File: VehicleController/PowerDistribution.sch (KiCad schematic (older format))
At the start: 22 parts, among them P3 RPi_USB_PWR, U10 BTS6133D, U11 R-78E5.0-1.0, U9 TL431

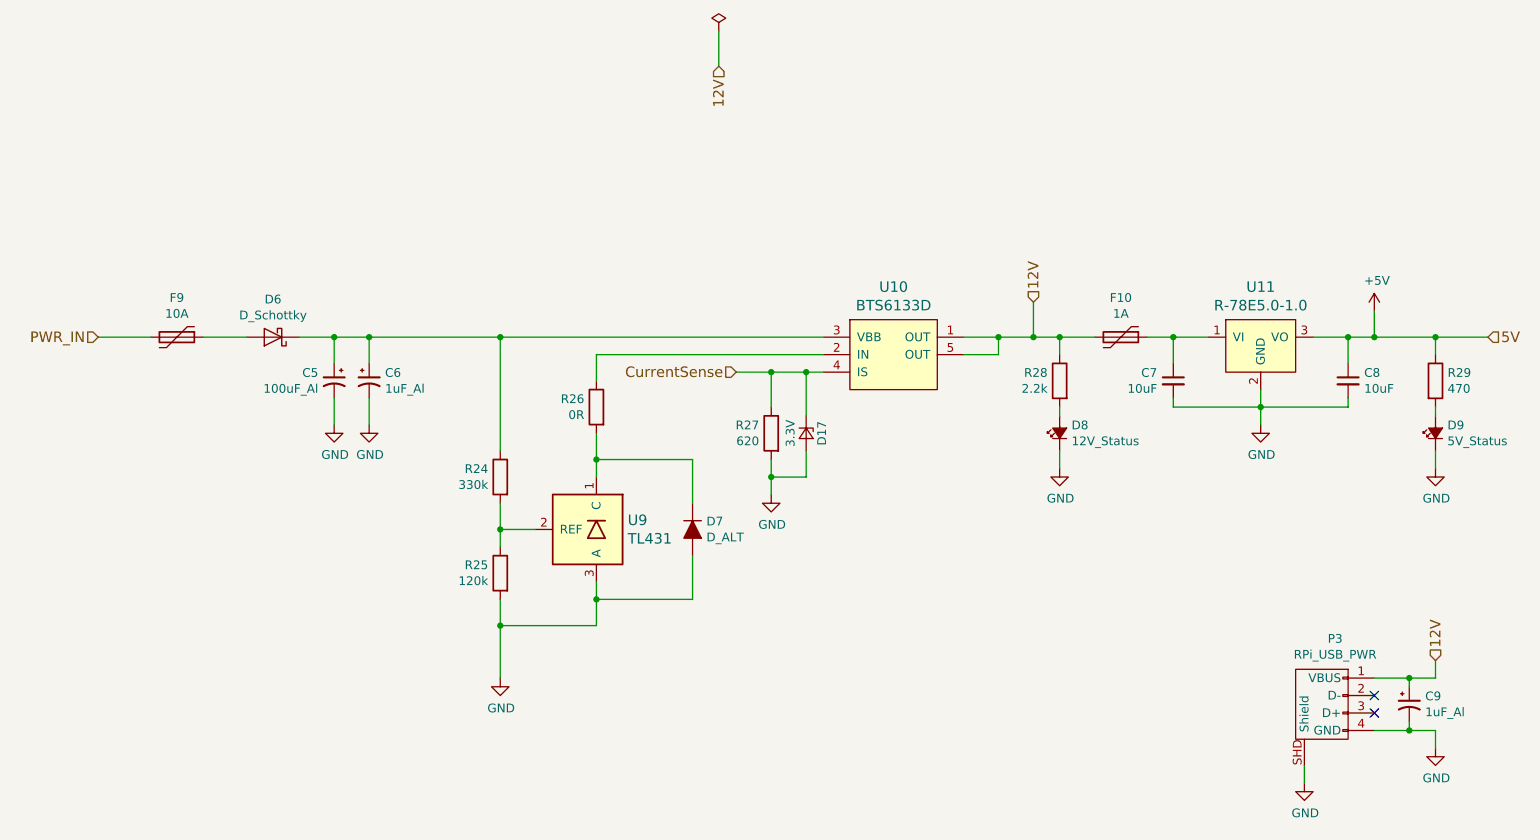
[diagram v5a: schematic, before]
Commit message: Fix Motor Controller Override circuit, better net names
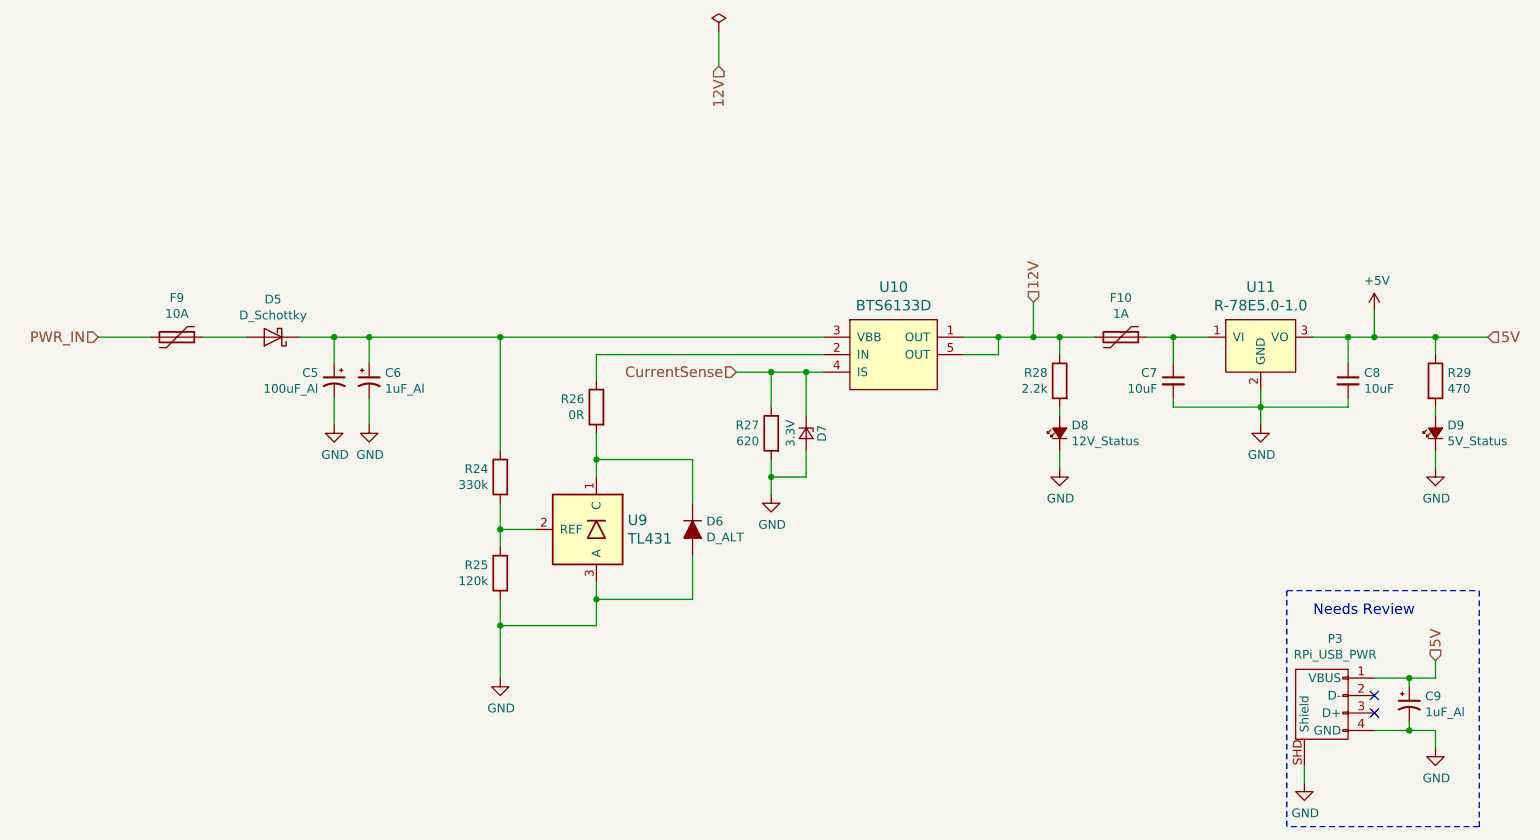
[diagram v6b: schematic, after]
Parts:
- renumbered D6 to D5, D7 to D6, D17 to D7
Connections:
- net +5V: now also C9.1, P3.1 (VBUS)
- net 12V: no longer C9.1, P3.1 (VBUS)
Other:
- note added: "Needs Review"
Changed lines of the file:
@@
 $EndDescr
 $Comp
-L D_Schottky D6
+L D_Schottky D5
 U 1 1 587C7BB2
 P 3000 2750
-F 0 "D6" H 3000 2534 50  0000 C CNN
+F 0 "D5" H 3000 2534 50  0000 C CNN
 F 1 "D_Schottky" H 3000 2625 50  0000 C CNN
 F 2 "Diodes_SMD:SMA_Handsoldering" H 3000 2750 50  0001 C CNN
@@
 $EndComp
 $Comp
-L GND #PWR41
+L GND #PWR042
 U 1 1 587C7BE3
 P 5850 3650
-F 0 "#PWR41" H 5850 3400 50  0001 C CNN
+F 0 "#PWR042" H 5850 3400 50  0001 C CNN
 F 1 "GND" H 5855 3477 50  0000 C CNN
 F 2 "" H 5850 3650 50  0000 C CNN
@@
 $EndComp
 $Comp
-L GND #PWR40
+L GND #PWR043
 U 1 1 587C7BF7
 P 4300 4700
-F 0 "#PWR40" H 4300 4450 50  0001 C CNN
+F 0 "#PWR043" H 4300 4450 50  0001 C CNN
 F 1 "GND" H 4305 4527 50  0000 C CNN
 F 2 "" H 4300 4700 50  0000 C CNN
@@
 $EndComp
 $Comp
-L GND #PWR43
+L GND #PWR044
 U 1 1 58AEB860
 P 8650 3250
-F 0 "#PWR43" H 8650 3000 50  0001 C CNN
+F 0 "#PWR044" H 8650 3000 50  0001 C CNN
 F 1 "GND" H 8655 3077 50  0000 C CNN
 F 2 "" H 8650 3250 50  0000 C CNN
@@
 5V
 $Comp
-L PWR_FLAG #FLG3
+L PWR_FLAG #FLG045
 U 1 1 58AF2028
 P 5550 1000
-F 0 "#FLG3" H 5550 1095 50  0001 C CNN
+F 0 "#FLG045" H 5550 1095 50  0001 C CNN
 F 1 "PWR_FLAG" H 5550 1224 50  0001 C CNN
 F 2 "" H 5550 1000 50  0000 C CNN
@@
 $EndComp
 $Comp
-L GND #PWR44
+L GND #PWR046
 U 1 1 58B30D9F
 P 8900 5300
-F 0 "#PWR44" H 8900 5050 50  0001 C CNN
+F 0 "#PWR046" H 8900 5050 50  0001 C CNN
 F 1 "GND" H 8905 5127 50  0000 C CNN
 F 2 "" H 8900 5300 50  0000 C CNN
@@
 NoConn ~ 9300 4800
 NoConn ~ 9300 4900
-Text HLabel 9650 4600 1    60   Input ~ 0
-12V
-$Comp
-L GND #PWR47
+$Comp
+L GND #PWR047
 U 1 1 58B31164
 P 9650 5100
-F 0 "#PWR47" H 9650 4850 50  0001 C CNN
+F 0 "#PWR047" H 9650 4850 50  0001 C CNN
 F 1 "GND" H 9655 4927 50  0000 C CNN
 F 2 "" H 9650 5100 50  0000 C CNN
@@
 $EndComp
 $Comp
-L GND #PWR38
+L GND #PWR048
 U 1 1 58B0EFE3
 P 3350 3250
-F 0 "#PWR38" H 3350 3000 50  0001 C CNN
+F 0 "#PWR048" H 3350 3000 50  0001 C CNN
 F 1 "GND" H 3355 3077 50  0000 C CNN
 F 2 "" H 3350 3250 50  0000 C CNN
@@
 $EndComp
 $Comp
-L GND #PWR39
+L GND #PWR049
 U 1 1 58B0F09D
 P 3550 3250
-F 0 "#PWR39" H 3550 3000 50  0001 C CNN
+F 0 "#PWR049" H 3550 3000 50  0001 C CNN
 F 1 "GND" H 3555 3077 50  0000 C CNN
 F 2 "" H 3550 3250 50  0000 C CNN
@@
 $EndComp
 $Comp
-L D_ALT D7
+L D_ALT D6
 U 1 1 58B90308
 P 5400 3850
-F 0 "D7" V 5354 3929 50  0000 L CNN
+F 0 "D6" V 5354 3929 50  0000 L CNN
 F 1 "D_ALT" V 5445 3929 50  0000 L CNN
 F 2 "Diodes_SMD:SMA_Handsoldering" H 5400 3850 50  0001 C CNN
@@
 	0    1    1    0
 $EndComp
-Wire Wire Line
-	5850 3150 5850 2950
-Wire Wire Line
-	5650 2950 6150 2950
-Wire Wire Line
-	4850 2850 6150 2850
-Wire Wire Line
-	3150 2750 6150 2750
-Wire Wire Line
-	4300 2750 4300 3400
-Connection ~ 4300 2750
-Wire Wire Line
-	5850 3450 5850 3650
-Wire Wire Line
-	4300 3700 4300 3950
-Wire Wire Line
-	4500 3850 4300 3850
-Connection ~ 4300 3850
-Wire Wire Line
-	2600 2750 2850 2750
-Wire Wire Line
-	2000 2750 2300 2750
-Wire Wire Line
-	4300 4250 4300 4700
-Wire Wire Line
-	4850 4400 4300 4400
-Wire Wire Line
-	4850 4150 4850 4400
-Connection ~ 4300 4400
-Wire Wire Line
-	6950 2850 7150 2850
-Wire Wire Line
-	7150 2850 7150 2750
-Connection ~ 7150 2750
-Connection ~ 5850 2950
-Wire Wire Line
-	8650 3050 8650 3250
-Wire Wire Line
-	8150 3100 8150 3150
-Wire Wire Line
-	8150 3150 9150 3150
-Connection ~ 8650 3150
-Wire Wire Line
-	9150 3150 9150 3100
-Wire Wire Line
-	8150 2750 8150 2900
-Wire Wire Line
-	6950 2750 7700 2750
-Wire Wire Line
-	8000 2750 8350 2750
-Wire Wire Line
-	9150 2900 9150 2750
-Wire Wire Line
-	8950 2750 9950 2750
-Connection ~ 8150 2750
-Connection ~ 9150 2750
-Wire Wire Line
-	7350 2750 7350 2550
-Connection ~ 7350 2750
-Wire Wire Line
-	5550 1200 5550 1000
-Connection ~ 9500 4700
-Wire Wire Line
-	9500 4750 9500 4700
-Connection ~ 9500 5000
-Wire Wire Line
-	9500 4950 9500 5000
-Wire Wire Line
-	9650 5000 9650 5100
-Wire Wire Line
-	9300 5000 9650 5000
-Wire Wire Line
-	8900 5300 8900 5200
-Wire Wire Line
-	9650 4700 9650 4600
-Wire Wire Line
-	9300 4700 9650 4700
-Wire Wire Line
-	3350 2900 3350 2750
-Connection ~ 3350 2750
-Wire Wire Line
-	3550 2900 3550 2750
-Connection ~ 3550 2750
-Wire Wire Line
-	3350 3250 3350 3100
-Wire Wire Line
-	3550 3250 3550 3100
-Wire Wire Line
-	5400 3700 5400 3450
-Wire Wire Line
-	5400 3450 4850 3450
-Connection ~ 4850 3450
-Wire Wire Line
-	5400 4000 5400 4250
-Wire Wire Line
-	5400 4250 4850 4250
-Connection ~ 4850 4250
-Wire Wire Line
-	4850 3300 4850 3550
-$Comp
-L +5V #PWR45
+$Comp
+L +5V #PWR050
 U 1 1 58BE7A1A
 P 9300 2600
-F 0 "#PWR45" H 9350 2650 50  0001 C CNN
+F 0 "#PWR050" H 9350 2650 50  0001 C CNN
 F 1 "+5V" H 9315 2773 50  0000 C CNN
 F 2 "" H 550 -100 50  0001 C CNN
@@
 	1    0    0    -1
 $EndComp
-Wire Wire Line
-	9300 2600 9300 2750
-Connection ~ 9300 2750
 $Comp
 L Polyfuse F10
@@
 	0    -1   -1   0
 $EndComp
-Wire Wire Line
-	7500 3150 7500 3200
-Wire Wire Line
-	7500 2850 7500 2750
-Connection ~ 7500 2750
-$Comp
-L GND #PWR42
+$Comp
+L GND #PWR051
 U 1 1 58C31B60
 P 7500 3500
-F 0 "#PWR42" H 7500 3250 50  0001 C CNN
+F 0 "#PWR051" H 7500 3250 50  0001 C CNN
 F 1 "GND" H 7505 3327 50  0000 C CNN
 F 2 "" H 7500 3500 50  0000 C CNN
@@
 	1    0    0    -1
 $EndComp
-Wire Wire Line
-	7500 3500 7500 3400
 $Comp
 L LED_Small_ALT D9
@@
 	1    0    0    -1
 $EndComp
-Wire Wire Line
-	9650 2850 9650 2750
-Connection ~ 9650 2750
-Wire Wire Line
-	9650 3200 9650 3150
-$Comp
-L GND #PWR46
+$Comp
+L GND #PWR052
 U 1 1 58C32364
 P 9650 3500
-F 0 "#PWR46" H 9650 3250 50  0001 C CNN
+F 0 "#PWR052" H 9650 3250 50  0001 C CNN
 F 1 "GND" H 9655 3327 50  0000 C CNN
 F 2 "" H 9650 3500 50  0000 C CNN
@@
 	1    0    0    -1
 $EndComp
-Wire Wire Line
-	9650 3500 9650 3400
 $Comp
 L CP1_Small C5
@@
 	-1   0    0    -1
 $EndComp
-Wire Wire Line
-	4850 3000 4850 2850
 $Comp
 L R-78E5.0-1.0 U11
@@
 	1    0    0    -1
 $EndComp
-Connection ~ 5850 3550
-$Comp
-L D_Zener_Small D17
+$Comp
+L D_Zener_Small D7
 U 1 1 58FBF2F0
 P 6050 3300
-F 0 "D17" H 6050 3390 50  0000 C CNN
+F 0 "D7" H 6050 3390 50  0000 C CNN
 F 1 "3.3V" H 6050 3210 50  0000 C CNN
 F 2 "" V 6050 3300 50  0001 C CNN
@@
 $EndComp
 Wire Wire Line
+	5850 3150 5850 2950
+Wire Wire Line
+	5650 2950 6150 2950
+Wire Wire Line
+	4850 2850 6150 2850
+Wire Wire Line
+	3150 2750 6150 2750
+Wire Wire Line
+	4300 2750 4300 3400
+Connection ~ 4300 2750
+Wire Wire Line
+	5850 3450 5850 3650
+Wire Wire Line
+	4300 3700 4300 3950
+Wire Wire Line
+	4500 3850 4300 3850
+Connection ~ 4300 3850
+Wire Wire Line
+	2600 2750 2850 2750
+Wire Wire Line
+	2000 2750 2300 2750
+Wire Wire Line
+	4300 4250 4300 4700
+Wire Wire Line
+	4850 4400 4300 4400
+Wire Wire Line
+	4850 4150 4850 4400
+Connection ~ 4300 4400
+Wire Wire Line
+	6950 2850 7150 2850
+Wire Wire Line
+	7150 2850 7150 2750
+Connection ~ 7150 2750
+Connection ~ 5850 2950
+Wire Wire Line
+	8650 3050 8650 3250
+Wire Wire Line
+	8150 3100 8150 3150
+Wire Wire Line
+	8150 3150 9150 3150
+Connection ~ 8650 3150
+Wire Wire Line
+	9150 3150 9150 3100
+Wire Wire Line
+	8150 2750 8150 2900
+Wire Wire Line
+	6950 2750 7700 2750
+Wire Wire Line
+	8000 2750 8350 2750
+Wire Wire Line
+	9150 2900 9150 2750
+Wire Wire Line
+	8950 2750 9950 2750
+Connection ~ 8150 2750
+Connection ~ 9150 2750
+Wire Wire Line
+	7350 2750 7350 2550
+Connection ~ 7350 2750
+Wire Wire Line
+	5550 1200 5550 1000
+Connection ~ 9500 4700
+Wire Wire Line
+	9500 4750 9500 4700
+Connection ~ 9500 5000
+Wire Wire Line
+	9500 4950 9500 5000
+Wire Wire Line
+	9650 5000 9650 5100
+Wire Wire Line
+	9300 5000 9650 5000
+Wire Wire Line
+	8900 5300 8900 5200
+Wire Wire Line
+	9650 4700 9650 4600
+Wire Wire Line
+	9300 4700 9650 4700
+Wire Wire Line
+	3350 2900 3350 2750
+Connection ~ 3350 2750
+Wire Wire Line
+	3550 2900 3550 2750
+Connection ~ 3550 2750
+Wire Wire Line
+	3350 3250 3350 3100
+Wire Wire Line
+	3550 3250 3550 3100
+Wire Wire Line
+	5400 3700 5400 3450
+Wire Wire Line
+	5400 3450 4850 3450
+Connection ~ 4850 3450
+Wire Wire Line
+	5400 4000 5400 4250
+Wire Wire Line
+	5400 4250 4850 4250
+Connection ~ 4850 4250
+Wire Wire Line
+	4850 3300 4850 3550
+Wire Wire Line
+	9300 2600 9300 2750
+Connection ~ 9300 2750
+Wire Wire Line
+	7500 3150 7500 3200
+Wire Wire Line
+	7500 2850 7500 2750
+Connection ~ 7500 2750
+Wire Wire Line
+	7500 3500 7500 3400
+Wire Wire Line
+	9650 2850 9650 2750
+Connection ~ 9650 2750
+Wire Wire Line
+	9650 3200 9650 3150
+Wire Wire Line
+	9650 3500 9650 3400
+Wire Wire Line
+	4850 3000 4850 2850
+Connection ~ 5850 3550
+Wire Wire Line
 	6050 3200 6050 2950
 Connection ~ 6050 2950
@@
 Wire Wire Line
 	6050 3550 5850 3550
+Text HLabel 9650 4600 1    60   Input ~ 0
+5V
+Text Notes 8950 4350 0    60   ~ 0
+Needs Review
+Wire Notes Line
+	8800 4200 9900 4200
+Wire Notes Line
+	9900 4200 9900 5550
+Wire Notes Line
+	9900 5550 8800 5550
+Wire Notes Line
+	8800 5550 8800 4200
 $EndSCHEMATC

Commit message: Small changes to VCU
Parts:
- removed C9: 1uF_Al, Capacitors_SMD:c_elec_4x5.3, symbol CP1_Small
- removed P3: RPi_USB_PWR, UNCAMotorsports:USB-A-THT, symbol USB_A-RESCUE-VehicleController
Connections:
- no-connect marks 2 -> 0
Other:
- note removed: "Needs Review"
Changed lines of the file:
@@
 12V
-$Comp
-L USB_A-RESCUE-VehicleController P3
-U 1 1 58B30D8B
-P 9000 4900
-F 0 "P3" V 8575 4824 50  0000 C CNN
-F 1 "RPi_USB_PWR" V 8666 4824 50  0000 C CNN
-F 2 "UNCAMotorsports:USB-A-THT" V 8950 4800 50  0001 C CNN
-F 3 "" V 8950 4800 50  0000 C CNN
-	1    9000 4900
-	0    -1   1    0
-$EndComp
-$Comp
-L GND #PWR46
-U 1 1 58B30D9F
-P 8900 5300
-F 0 "#PWR46" H 8900 5050 50  0001 C CNN
-F 1 "GND" H 8905 5127 50  0000 C CNN
-F 2 "" H 8900 5300 50  0000 C CNN
-F 3 "" H 8900 5300 50  0000 C CNN
-	1    8900 5300
-	1    0    0    -1
-$EndComp
-NoConn ~ 9300 4800
-NoConn ~ 9300 4900
-$Comp
-L GND #PWR49
-U 1 1 58B31164
-P 9650 5100
-F 0 "#PWR49" H 9650 4850 50  0001 C CNN
-F 1 "GND" H 9655 4927 50  0000 C CNN
-F 2 "" H 9650 5100 50  0000 C CNN
-F 3 "" H 9650 5100 50  0000 C CNN
-	1    9650 5100
-	1    0    0    -1
-$EndComp
 $Comp
 L GND #PWR40
@@
 $EndComp
 $Comp
-L CP1_Small C9
-U 1 1 58C289B7
-P 9500 4850
-F 0 "C9" H 9591 4896 50  0000 L CNN
-F 1 "1uF_Al" H 9591 4805 50  0000 L CNN
-F 2 "Capacitors_SMD:c_elec_4x5.3" H 0   0   50  0001 C CNN
-F 3 "" H 0   0   50  0001 C CNN
-	1    9500 4850
-	1    0    0    -1
-$EndComp
-$Comp
 L D_Zener_Small D7
 U 1 1 58FBF2F0
@@
 Wire Wire Line
 	5550 1200 5550 1000
-Connection ~ 9500 4700
-Wire Wire Line
-	9500 4750 9500 4700
-Connection ~ 9500 5000
-Wire Wire Line
-	9500 4950 9500 5000
-Wire Wire Line
-	9650 5000 9650 5100
-Wire Wire Line
-	9300 5000 9650 5000
-Wire Wire Line
-	8900 5300 8900 5200
-Wire Wire Line
-	9650 4700 9650 4600
-Wire Wire Line
-	9300 4700 9650 4700
 Wire Wire Line
 	3350 2900 3350 2750
@@
 Wire Wire Line
 	6050 3550 5850 3550
-Text HLabel 9650 4600 1    60   Input ~ 0
-5V
-Text Notes 8950 4350 0    60   ~ 0
-Needs Review
-Wire Notes Line
-	8800 4200 9900 4200
-Wire Notes Line
-	9900 4200 9900 5550
-Wire Notes Line
-	9900 5550 8800 5550
-Wire Notes Line
-	8800 5550 8800 4200
 $EndSCHEMATC
